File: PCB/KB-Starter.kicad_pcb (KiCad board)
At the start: 2 copper layers, 97.1 x 101.4 mm, 67 parts, among them J1 USB_C_Receptacle_USB2.0, J2 SWD, SW1 SW_Push, U1 W25Q128JVS, U2 USBLC6-2SC6, U3 XC6206PxxxMR, U5 RP2040, Y1 12MHz

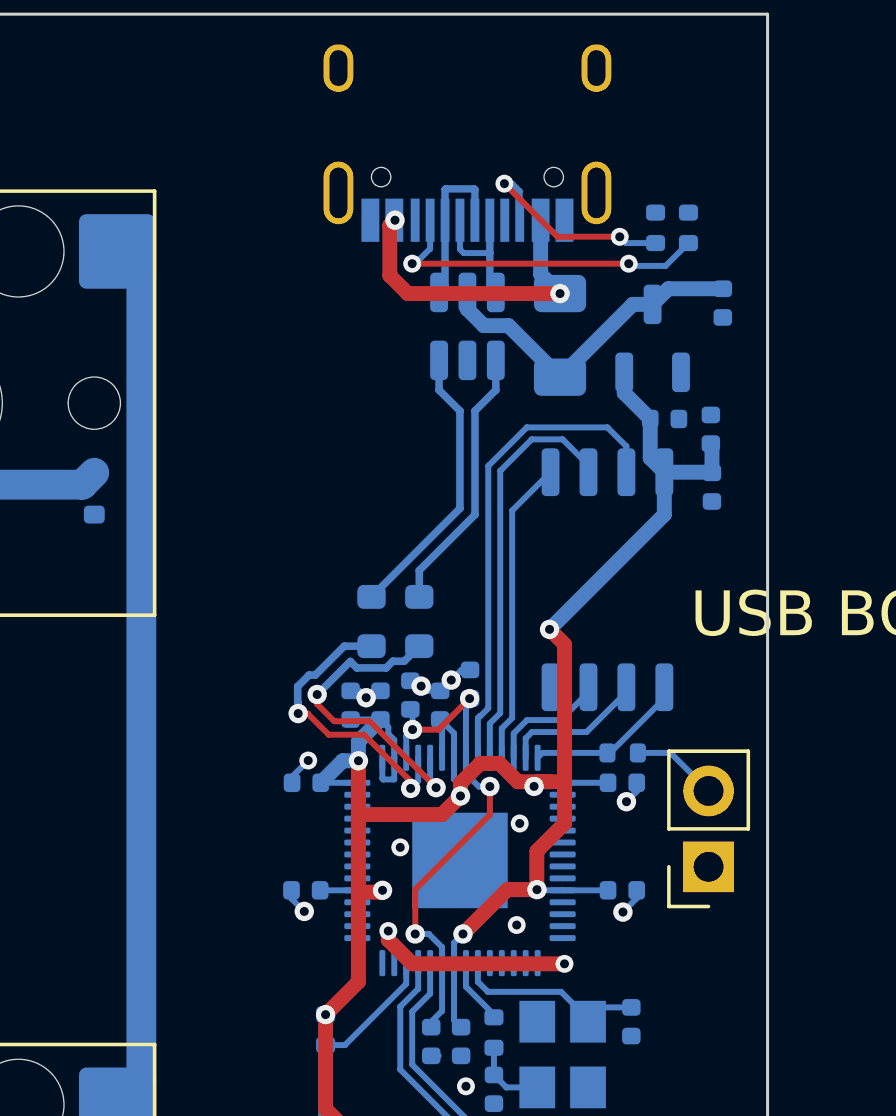
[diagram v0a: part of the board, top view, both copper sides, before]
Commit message: fix: USB data line impedance and length
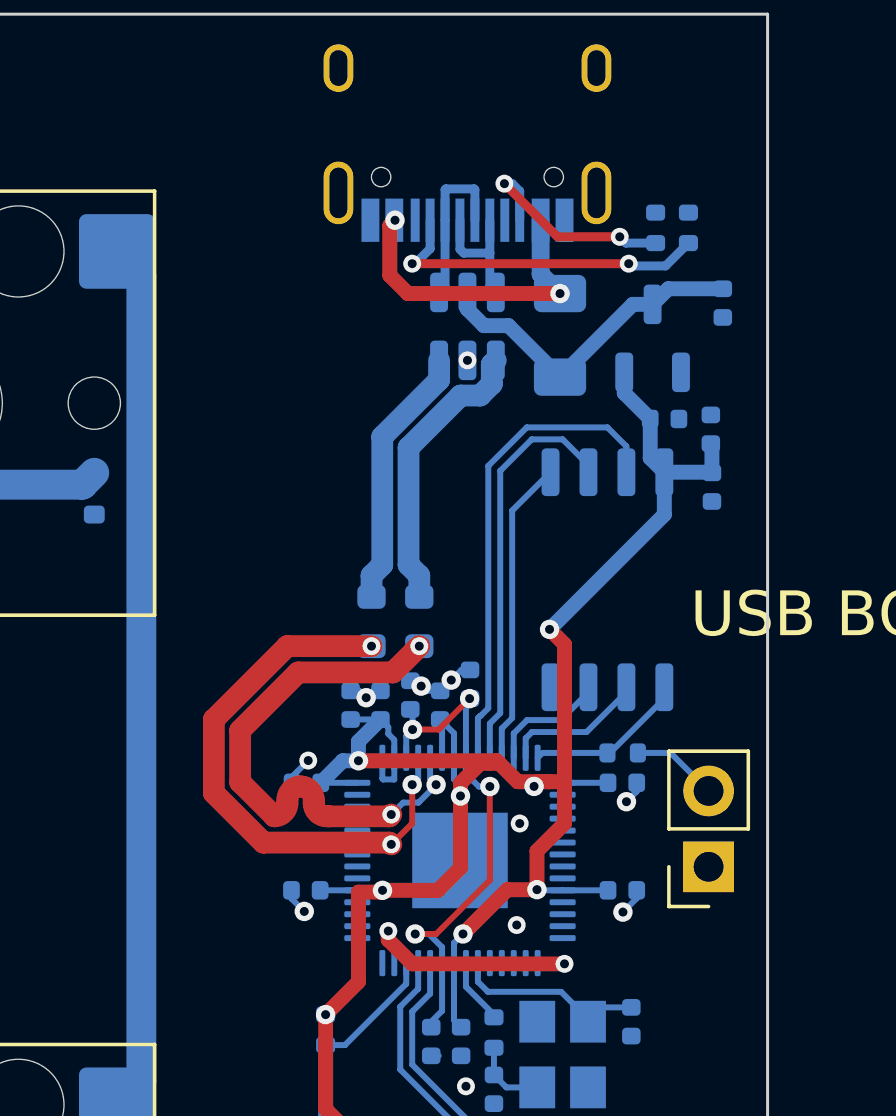
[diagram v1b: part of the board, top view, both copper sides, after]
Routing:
- net USBD_N: track 10.0 -> 18.7 mm, vias 2 -> 3
- net USBD_P: track 10.8 -> 18.5 mm, vias 2 -> 3
- net +3V3: track 74.1 -> 76.1 mm
- net D_P: track 8.98 -> 9.66 mm
- net D_N: track 9.44 -> 8.86 mm

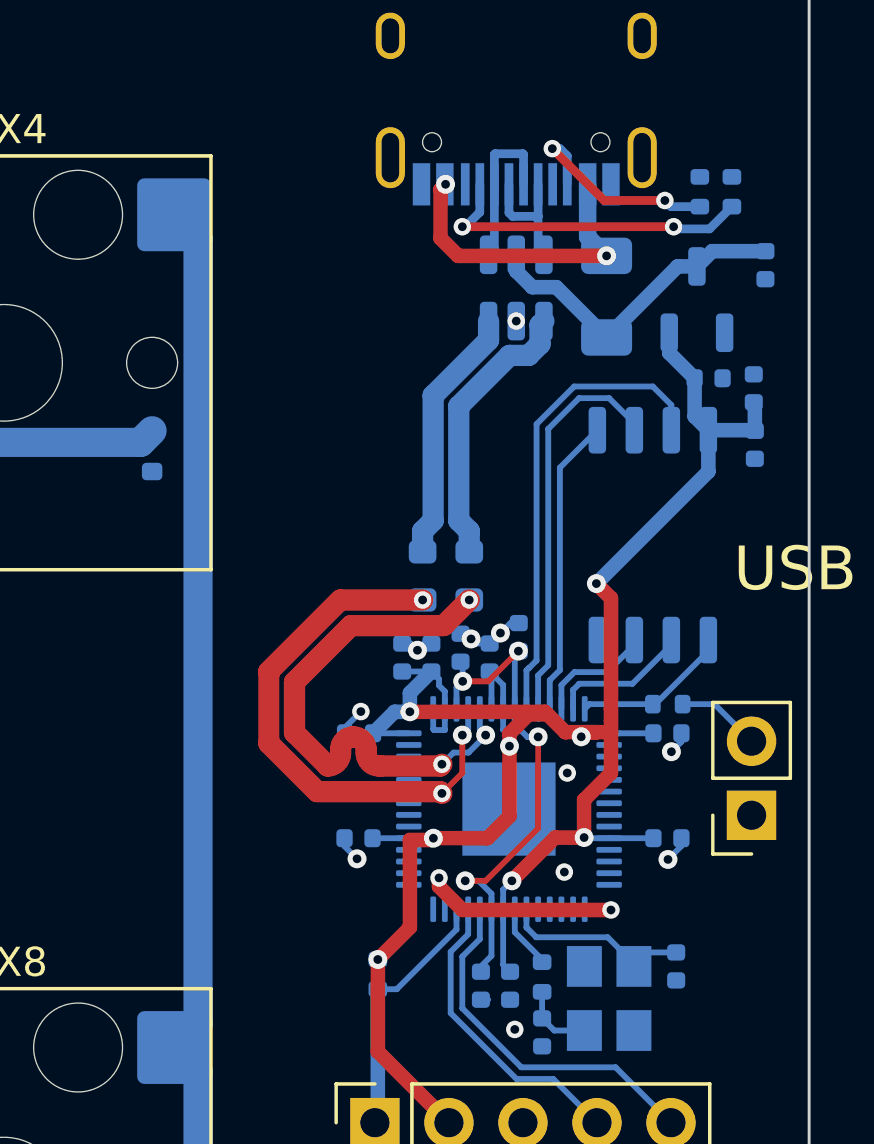
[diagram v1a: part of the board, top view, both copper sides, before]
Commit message: fix: reduce via-in-pads
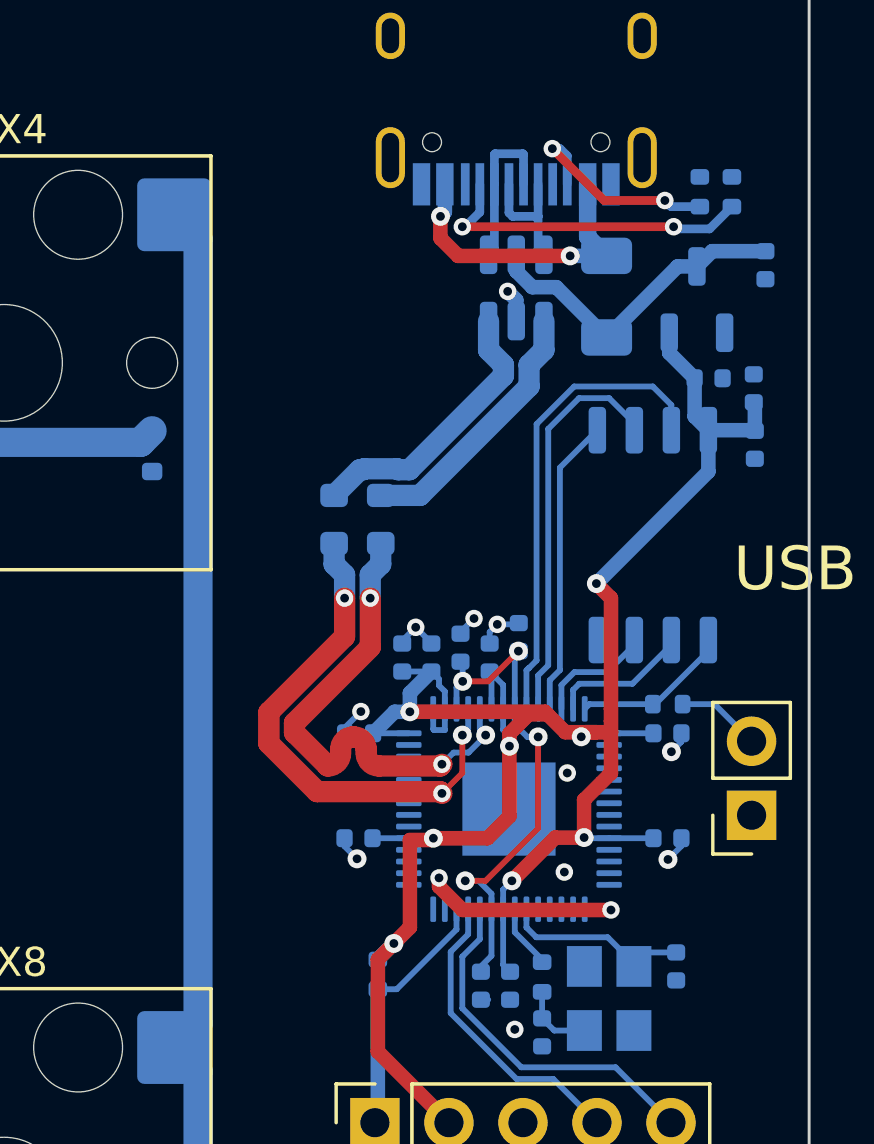
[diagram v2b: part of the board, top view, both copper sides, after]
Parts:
- moved R5 3.60 mm to (104.6, 39.9)
- moved R6 3.60 mm to (103.0, 39.9)
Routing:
- net GND: track 14.0 -> 15.2 mm
- net USBD_P: track 18.5 -> 17.4 mm
- net +3V3: track 76.1 -> 76.9 mm
- net D_N: track 8.86 -> 9.63 mm
- net USBD_N: track 18.7 -> 18.0 mm
- net D_P: track 9.66 -> 9.09 mm

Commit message: fix+feat: matrix fix + touchup
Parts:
- SW1: footprint Connector_PinSocket_2.54mm:PinSocket_1x02_P2.54mm_Vertical -> Button_Switch_SMD:SW_SPST_FSMSM
- moved SW1 17.2 mm to (107.7, 35.9), turned to 0 degrees
- moved C10 1.05 mm to (107.3, 44.6)
- moved C11 1.05 mm to (104.3, 44.6)
- moved C15 1.05 mm to (102.8, 50.8)
- moved C4 1.05 mm to (106.3, 44.2)
- moved C5 1.05 mm to (108.3, 43.9)
- moved C7 1.05 mm to (116.3, 35.3)
- moved C8 1.05 mm to (105.3, 44.6)
- moved J2 1.05 mm to (103.3, 60.5)
- moved R1 1.05 mm to (113.4, 46.2)
- moved R3 1.05 mm to (115.6, 28.6)
- moved D10 1.05 mm to (57.6, 75.6)
- moved D2 1.05 mm to (57.6, 37.5)
- moved D6 1.05 mm to (57.6, 56.5)
- moved MX2 1.05 mm to (52.5, 34.5)
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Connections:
- MX15 pad 2: Net-(MX15-Pad2) -> COL4
- MX4 pad 2: Net-(MX15-Pad2) -> COL4
- MX8 pad 2: Net-(MX15-Pad2) -> COL4
- U5 pad 11: COL3 -> COL4
- U5 pad 7: /GPIO5 -> COL1
- U5 pad 8: COL1 -> COL2
- U5 pad 9: COL2 -> COL3
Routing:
- net ROW4: track 0.00 -> 137.1 mm, vias 0 -> 5
- net ROW5: track 0.00 -> 128.2 mm, vias 0 -> 5
- net ROW1: track 0.00 -> 125.4 mm, vias 0 -> 5
- net COL4: track 0.00 -> 117.6 mm, vias 0 -> 2
- net COL1: track 82.2 -> 196.3 mm, vias 0 -> 2
- net ROW2: track 0.00 -> 105.0 mm, vias 0 -> 5
- net ROW3: track 0.00 -> 104.9 mm, vias 0 -> 4
- net COL2: track 59.2 -> 152.2 mm, vias 0 -> 2
- net COL3: track 78.9 -> 147.9 mm, vias 0 -> 2
- net Net-(MX15-Pad2): track 68.0 -> 0.00 mm
- net /~{USB_BOOT}: track 2.89 -> 16.5 mm, vias 0 -> 1
- net USBD_P: track 17.4 -> 17.2 mm, vias 3 -> 2
- net USBD_N: vias 3 -> 2
- net GND: vias 13 -> 12
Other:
- board size 97.1 x 101.4 mm -> 100.1 x 104.6 mm

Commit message: feat: stabs
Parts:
- added REF**: Stabilizer_Cherry_MX_2.00u, PCM_Mounting_Keyboard_Stabilizer:Stabilizer_Cherry_MX_2.00u, F.Cu at (90.6, 63.0)
- added REF**: Stabilizer_Cherry_MX_2.00u, PCM_Mounting_Keyboard_Stabilizer:Stabilizer_Cherry_MX_2.00u, F.Cu at (90.6, 101.1)
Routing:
- net COL4: track 117.6 -> 122.7 mm
- net ROW1: track 125.4 -> 126.7 mm

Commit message: fix: old footprints
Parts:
- moved C7 1.99 mm to (116.8, 33.4), turned to -90 degrees
- moved J1 0.09 mm to (108.2, 24.2)
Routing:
- net +3V3: track 77.0 -> 80.0 mm
- net D_USB_P: track 4.53 -> 5.46 mm
- net /CC1: track 11.4 -> 12.3 mm
- net COL4: track 122.7 -> 123.3 mm
- net COL3: track 147.9 -> 148.5 mm

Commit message: add missing 3d models, cleanup for KiCad 8, swd
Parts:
- added STAB1: Stabilizer_Cherry_MX_2.00u, PCM_Mounting_Keyboard_Stabilizer:Stabilizer_Cherry_MX_2.00u, F.Cu at (43.0, 110.7)
- J2: value SWD -> 3-pin SWD; footprint Connector_PinSocket_2.54mm:PinSocket_1x05_P2.54mm_Vertical -> Connector_JST:JST_SH_SM03B-SRSS-TB_1x03-1MP_P1.00mm_Horizontal
- MX1, MX10, MX11, MX13, MX14, MX17, MX2, MX3, MX4, MX5, MX6, MX7, MX9: value SW_Push -> Kailh Hotswap
- MX12, MX15, MX8: value SW_Push -> Kailh Hotswap; footprint PCM_Switch_Keyboard_Hotswap_Kailh:SW_Hotswap_Kailh_MX_2.00u_90deg -> PCM_Switch_Keyboard_Hotswap_Kailh:SW_Hotswap_Kailh_MX_1.00u
- MX16: value SW_Push -> Kailh Hotswap; footprint PCM_Switch_Keyboard_Hotswap_Kailh:SW_Hotswap_Kailh_MX_2.00u -> PCM_Switch_Keyboard_Hotswap_Kailh:SW_Hotswap_Kailh_MX_1.00u
- SW1: footprint Button_Switch_SMD:SW_SPST_FSMSM -> Button_Switch_SMD:SW_SPST_PTS810
- moved R3 11.6 mm to (104.1, 30.2), turned to 0 degrees
- moved R4 10.7 mm to (104.1, 31.2), turned to 0 degrees
- moved R6 4.05 mm to (105.9, 40.6)
- moved R5 3.97 mm to (107.4, 40.6)
- moved J2 3.86 mm to (106.7, 62.5), turned to 0 degrees
- moved R2 1.68 mm to (104.9, 54.6), turned to 0 degrees
- moved C2 1.50 mm to (113.7, 56.7)
- moved C5 1.04 mm to (108.7, 42.9)
- moved C4 0.55 mm to (106.3, 43.7)
- moved C17 0.50 mm to (114.3, 35.1), turned to 0 degrees
- moved Y1 0.37 mm to (111.4, 56.6)
- moved SW1 0.31 mm to (107.4, 36.1)
- moved C13 0.08 mm to (113.5, 50.8)
- turned C7 to 90 degrees
- turned STAB2 to 90 degrees
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- renumbered REF** to STAB2, REF** to STAB3
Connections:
- J2 pad 1: ~{RESET} -> SWD
- J2 pad 2: +3V3 -> GND
- J2 pad 3: GND -> SWCLK
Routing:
- net GND: track 15.2 -> 3.88 mm, vias 12 -> 18
- net +3V3: track 80.0 -> 69.5 mm
- net USBD_N: track 18.0 -> 7.50 mm
- net USBD_P: track 17.2 -> 7.45 mm
- net /CC1: track 12.3 -> 4.66 mm
- net ~{RESET}: track 8.86 -> 1.70 mm
- net COL3: track 148.5 -> 142.4 mm
- net COL2: track 152.6 -> 147.4 mm
- net COL1: track 196.7 -> 191.5 mm
- net SWCLK: track 12.4 -> 7.98 mm, vias 0 -> 1
- net COL4: track 123.3 -> 119.1 mm
- net /~{USB_BOOT}: track 16.5 -> 20.5 mm
- net /CC2: track 7.52 -> 10.3 mm
- net SWD: track 10.4 -> 7.62 mm, vias 0 -> 1
- net ROW1: track 126.7 -> 124.5 mm
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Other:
- board text removed: "3V3"
- board text removed: "GND"
- board text removed: "SWCLK"
- board text removed: "~{RESET}"

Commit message: feat: cleanup, graphics, JLCPCB DRU
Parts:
- added J3: 3-pin UART, Connector_JST:JST_SH_BM03B-SRSS-TB_1x03-1MP_P1.00mm_Vertical, B.Cu at (103.0, 68.5)
- added R10: 100, Resistor_SMD:R_0603_1608Metric, B.Cu at (102.2, 56.3)
- added R11: 100, Resistor_SMD:R_0603_1608Metric, B.Cu at (100.5, 56.3)
- added R8: 100, Resistor_SMD:R_0603_1608Metric, B.Cu at (99.2, 53.1)
- added R9: 100, Resistor_SMD:R_0603_1608Metric, B.Cu at (97.4, 53.1)
- J2: footprint Connector_JST:JST_SH_SM03B-SRSS-TB_1x03-1MP_P1.00mm_Horizontal -> Connector_JST:JST_SH_BM03B-SRSS-TB_1x03-1MP_P1.00mm_Vertical; moved to B.Cu
- SW1: moved to B.Cu
- moved SW1 18.9 mm to (111.6, 54.5), turned to -90 degrees
- moved D14 6.50 mm to (71.7, 90.4)
- moved D17 6.50 mm to (71.7, 109.5)
- moved MX11 6.50 mm to (66.6, 68.4)
- moved MX14 6.50 mm to (66.6, 87.4)
- moved MX17 6.50 mm to (66.6, 106.5)
- moved C1 6.50 mm to (97.8, 43.0)
- moved C12 6.50 mm to (108.4, 43.0)
- moved C3 6.50 mm to (104.1, 53.2)
- moved C5 6.50 mm to (103.8, 38.7)
- moved C9 6.50 mm to (111.4, 33.1)
- moved D3 6.50 mm to (71.7, 33.3)
- moved MX7 6.50 mm to (66.6, 49.3)
- moved R2 6.50 mm to (99.9, 50.4)
- moved R6 6.50 mm to (101.0, 36.4)
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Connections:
- J2 pad 1: SWD -> Net-(J2-Pin_1)
- J2 pad 3: SWCLK -> Net-(J2-Pin_3)
- J2 pad MP: (no net) -> GND
- U5 pad 31: /GPIO20 -> UART0_TX
- U5 pad 32: /GPIO21 -> UART0_RX
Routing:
- net Net-(J3-Pin_1): track 0.00 -> 18.2 mm
- net Net-(J3-Pin_3): track 0.00 -> 15.3 mm
- net ROW1: track 124.5 -> 136.1 mm
- net ROW2: track 105.0 -> 113.3 mm
- net UART0_RX: track 0.00 -> 6.69 mm
- net UART0_TX: track 0.00 -> 6.68 mm
- net Net-(J2-Pin_1): track 0.00 -> 6.57 mm
- net Net-(J2-Pin_3): track 0.00 -> 3.85 mm
- net ROW3: track 104.9 -> 108.1 mm
- net /~{USB_BOOT}: track 20.5 -> 17.9 mm, vias 1 -> 0
- net COL4: track 119.1 -> 116.6 mm
- net SWCLK: track 7.98 -> 6.95 mm, vias 1 -> 0
- net SWD: track 7.62 -> 6.89 mm, vias 1 -> 0
- net GND: vias 18 -> 33
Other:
- board size 100.1 x 104.6 mm -> 99.3 x 103.6 mm
- board text added: "BOOT"
- board text added: "PCB3D_BR_KB_STARTER"
- board text added: "PCB3D_TL_KB_STARTER"
- board text added: "UART"
- board text removed: "USB BOOT"
